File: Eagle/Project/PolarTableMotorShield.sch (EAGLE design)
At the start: 5 parts, among them U8 CD74HC4094M96

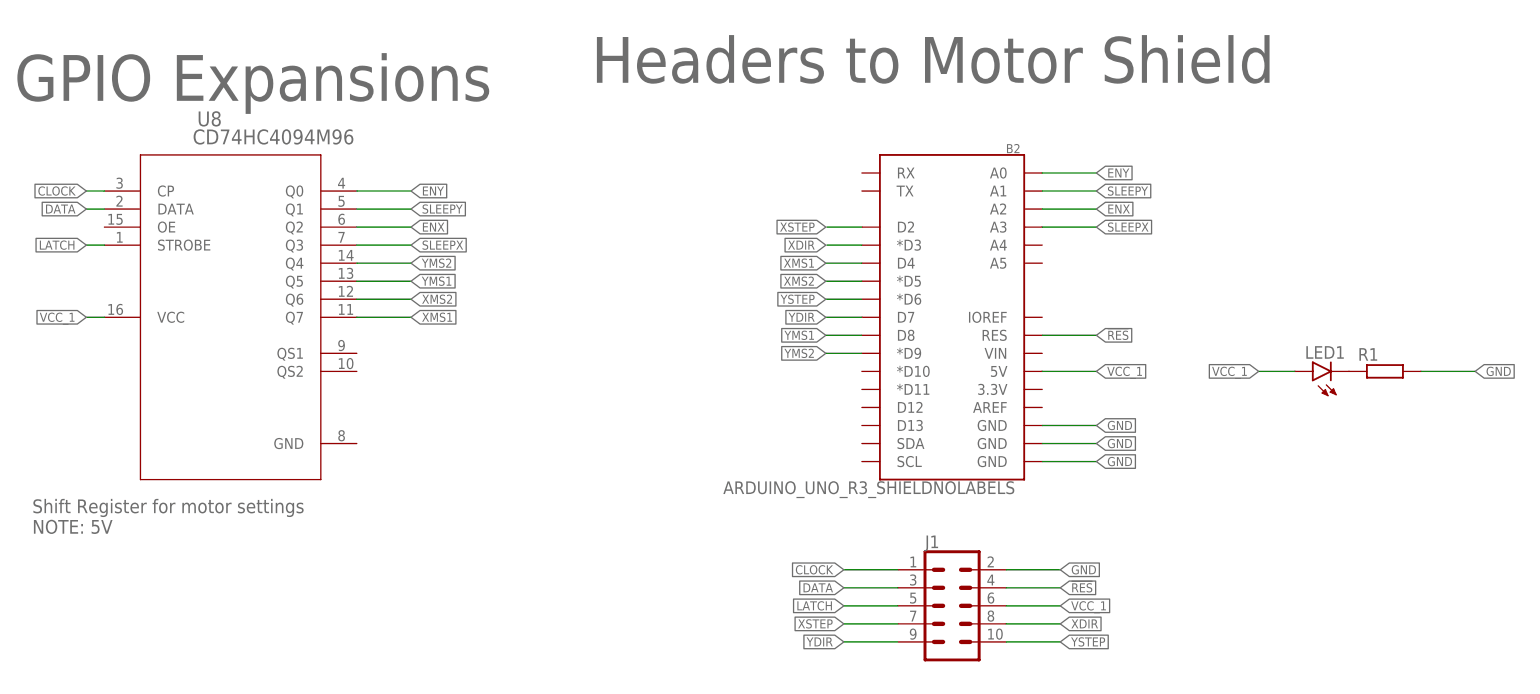
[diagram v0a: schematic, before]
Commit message: Changed the connector to be 6x2 so the shift reg could run at 3.3V
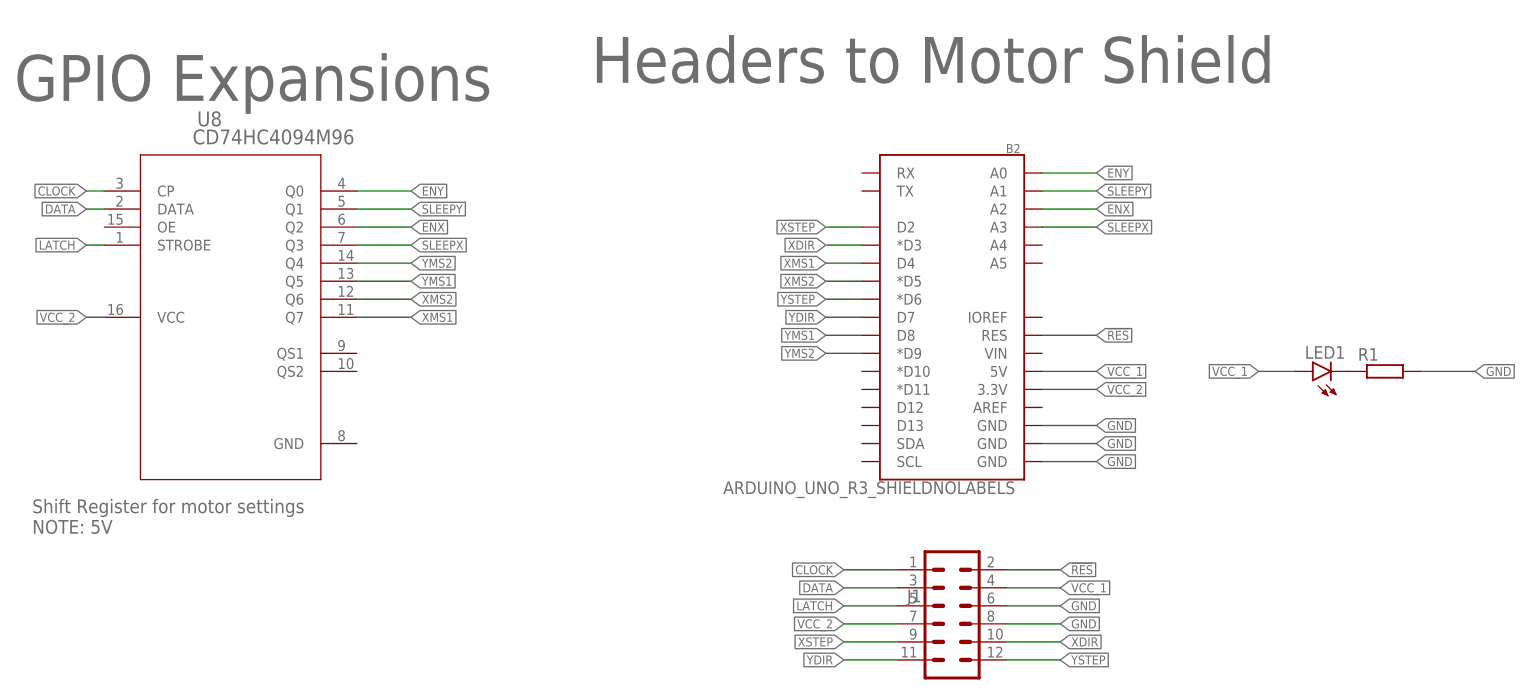
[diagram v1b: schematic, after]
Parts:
- J1: device SparkFun-Connectors:CONN_05X2RA -> keir_library:CONN_06X21.24MM_RA_MALE
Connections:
- new net VCC_2: B2.3.3V, J1.7, U8.VCC
- net !RES: now also J1.2; no longer J1.4
- net GND: now also J1.6, J1.8; no longer J1.2
- net VCC_1: now also J1.4; no longer J1.6, U8.VCC
- net XDIR: now also J1.10; no longer J1.8
- net XSTEP: now also J1.9; no longer J1.7
- net YDIR: now also J1.11; no longer J1.9
- net YSTEP: now also J1.12; no longer J1.10
